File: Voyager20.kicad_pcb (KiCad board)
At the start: 2 copper layers, 73 x 95.2 mm, 92 parts, among them Q1 Q_NPN_BEC, SW1 SW_Push, U1 ATmega32U2-AU, U2 PRTR5V0U2X, Y1 16MHz

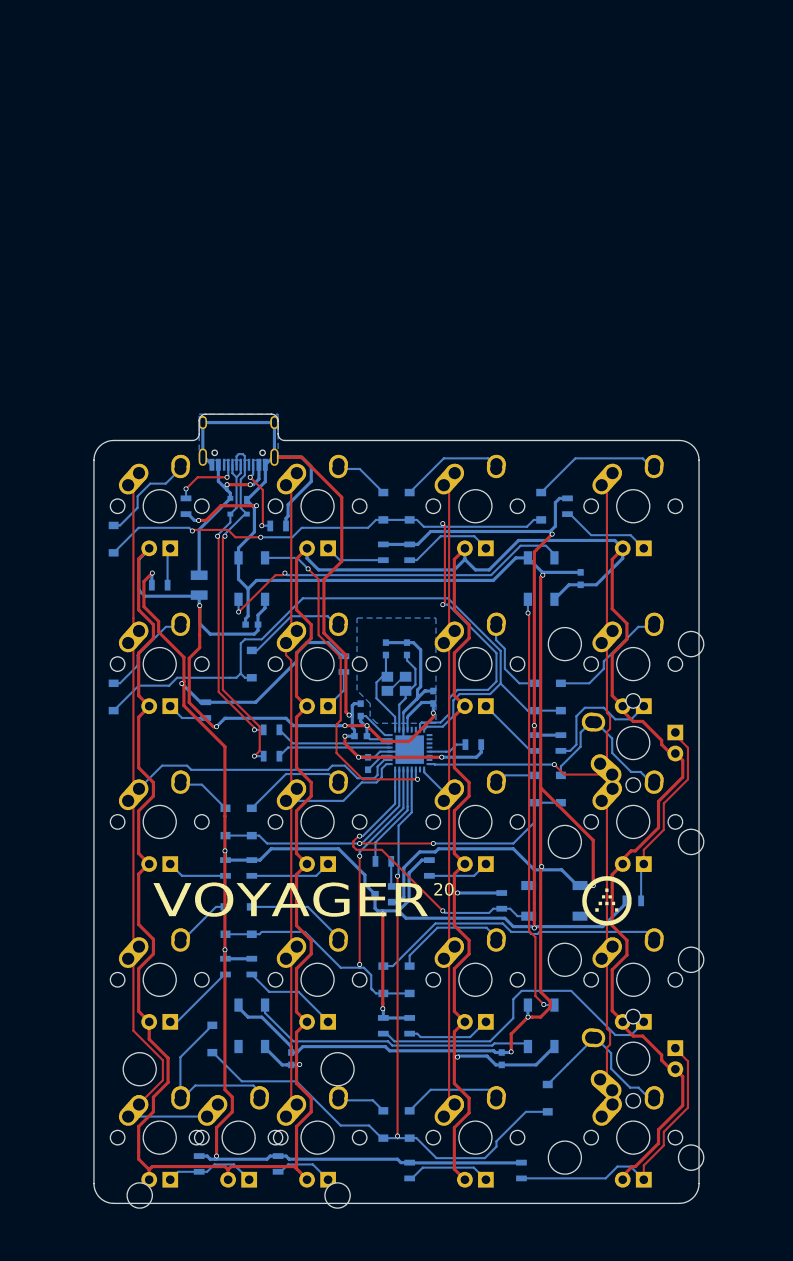
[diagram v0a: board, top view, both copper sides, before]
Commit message: Make 24 key variant
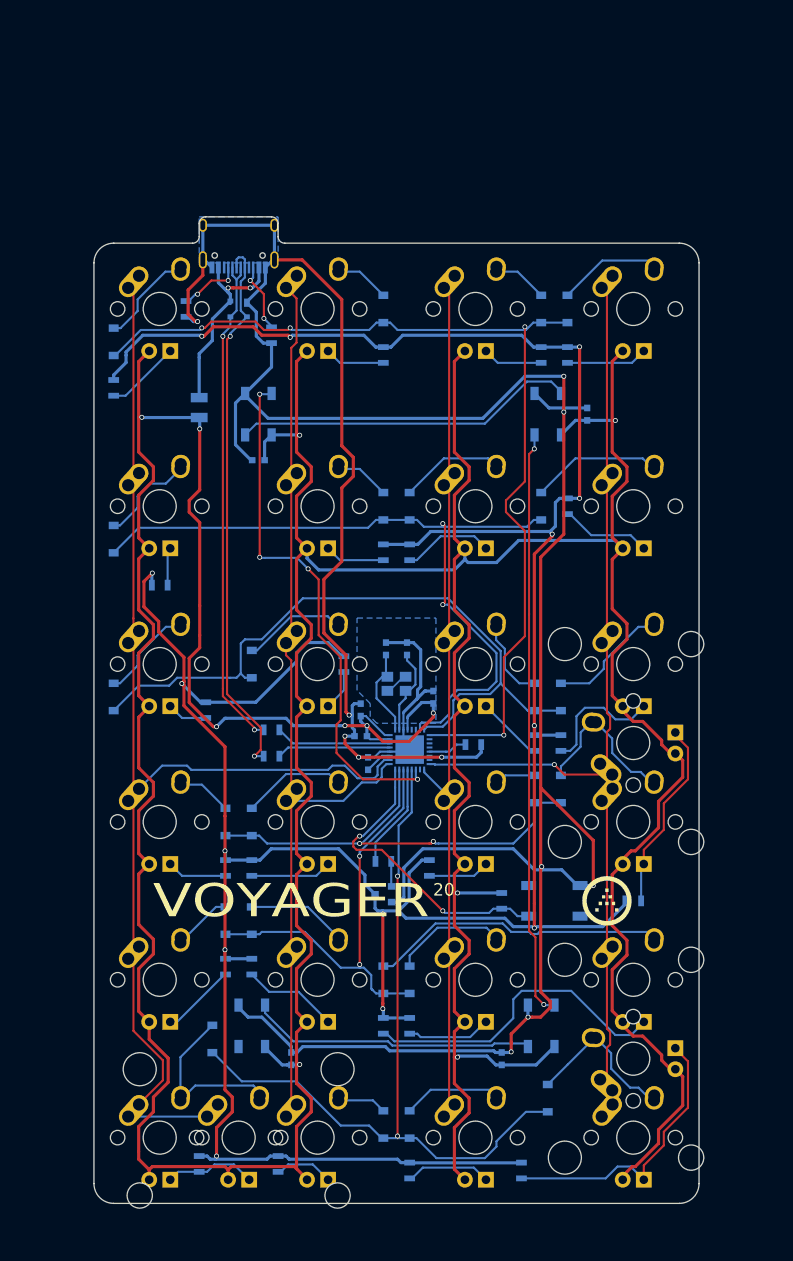
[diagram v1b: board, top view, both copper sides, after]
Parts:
- added D25: SOD-123, Diodes_SMD:D_SOD-123, B.Cu at (42.1, 19.8)
- added D26: SOD-123, Diodes_SMD:D_SOD-123, B.Cu at (74.6, 15.9)
- added D27: SOD-123, Diodes_SMD:D_SOD-123, B.Cu at (93.7, 15.9)
- added D28: SOD-123, Diodes_SMD:D_SOD-123, B.Cu at (96.8, 15.9)
- added MX21: MX-1U, MX_Alps_Hybrid:MX-1U, F.Cu at (47.6, 15.9)
- added MX22: MX-1U, MX_Alps_Hybrid:MX-1U, F.Cu at (66.7, 15.9)
- added MX23: MX-1U, MX_Alps_Hybrid:MX-1U, F.Cu at (85.7, 15.9)
- added MX24: MX-1U, MX_Alps_Hybrid:MX-1U, F.Cu at (104.8, 15.9)
- added R28: 1k, Resistors_SMD:R_0805, B.Cu at (42.1, 25.4)
- added R29: 1k, Resistors_SMD:R_0805, B.Cu at (74.6, 21.4)
- added R30: 1k, Resistors_SMD:R_0805, B.Cu at (93.7, 21.4)
- added R31: 1k, Resistors_SMD:R_0805, B.Cu at (96.8, 21.4)
- moved R6 23.8 mm to (50.8, 15.9)
- moved U2 23.8 mm to (57.1, 15.9)
- moved USB1 23.8 mm to (57.1, 3.17)
- moved R4 23.0 mm to (61.1, 19.1), turned to 270 degrees
- moved F1 21.4 mm to (52.4, 27.8)
- moved CR2 19.9 mm to (99.2, 28.6)
- moved D18 19.9 mm to (94.5, 28.6)
- moved D9 19.9 mm to (59.5, 28.6)
- moved CR1 19.9 mm to (59.5, 34.1)
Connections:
- U1 pad 9: Net-(U1-Pad9) -> ROWFN
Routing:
- net ROWFN: track 0.00 -> 119.8 mm, vias 0 -> 4
- net +5V: track 547.6 -> 658.1 mm, vias 8 -> 11
- net LEDGND: track 308.1 -> 390.4 mm, vias 10 -> 14
- net GND: track 345.4 -> 396.1 mm
- net COL1: track 93.3 -> 118.1 mm
- net COL0: track 123.3 -> 147.7 mm
- net COL2: track 83.1 -> 107.4 mm
- net COL3: track 100.1 -> 124.4 mm
- net Net-(R3-Pad1): track 43.5 -> 66.7 mm
- net Net-(R2-Pad2): track 37.8 -> 61.0 mm
- net RGBLED: track 42.2 -> 64.0 mm, vias 2 -> 4
- net Net-(D18-Pad2): track 51.0 -> 71.1 mm
- net Net-(D28-Pad2): track 0.00 -> 13.3 mm
- net Net-(D25-Pad2): track 0.00 -> 11.7 mm
- net Net-(MX24-Pad4): track 0.00 -> 9.80 mm
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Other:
- board size 73 x 95.2 mm -> 73 x 119.1 mm

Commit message: Route 3700 variant
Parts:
- removed CR1, CR2, CR3, CR4: 0.1u, Capacitors_SMD:C_0603
- removed D18, D23, D24, D9: WS2812B, LEDs:LED_WS2812B-PLCC4
- removed R4, R6: 5.1k, Resistors_SMD:R_0805
- removed USB1: HRO-TYPE-C-31-M-12, Type-C:HRO-TYPE-C-31-M-12-Assembly
- added J1: Conn_01x04, Pin_Headers:Pin_Header_Straight_1x04_Pitch2.54mm, B.Cu at (53.2, -13.5)
- added JP1: JP-INDICATOR, random-keyboard-parts:Jumper-UserFriendly-Small, B.Cu at (54.0, 49.2)
- added JP2: JP-BLIGHT, random-keyboard-parts:Jumper-UserFriendly-Small, B.Cu at (57.1, 49.2)
- added REF**: outline, locallib:outline, F.Cu at (30.4, -19.3)
- added REF**: MountingHole_3.2mm_M3, Mounting_Holes:MountingHole_3.2mm_M3, F.Cu at (71.4, -15.1)
- added REF**: MountingHole_3.2mm_M3, Mounting_Holes:MountingHole_3.2mm_M3, F.Cu at (81.0, -15.1)
- U1: footprint Housings_DFN_QFN:QFN-32-1EP_5x5mm_Pitch0.5mm -> Housings_QFP:TQFP-32_7x7mm_Pitch0.8mm
- moved Q1 101.4 mm to (45.5, -10.6)
- moved R27 101.4 mm to (45.5, -14.6)
- moved SW1 84.2 mm to (43.7, 20.7), turned to 90 degrees
- moved R1 74.7 mm to (43.7, 27.8), turned to 0 degrees
- moved G*** 72.1 mm to (111.1, 15.9)
- moved R3 63.0 mm to (55.6, 7.14), turned to 270 degrees
- moved C3 62.3 mm to (54.8, 11.1), turned to 0 degrees
- moved R2 59.6 mm to (58.7, 7.14), turned to 90 degrees
- moved C5 55.5 mm to (62.7, 12.7), turned to 0 degrees
- moved C6 54.7 mm to (62.7, 10.3), turned to 0 degrees
- moved U1 54.1 mm to (56.9, 19.1), turned to 180 degrees
- moved R5 49.4 mm to (56.4, 28.6), turned to 90 degrees
- moved Y1 45.7 mm to (66.8, 16.4), turned to 270 degrees
- moved C4 43.6 mm to (66.7, 21.4), turned to 0 degrees
- moved C1 41.9 mm to (71.0, 15.2), turned to 0 degrees
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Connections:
- net Net-(MX1-Pad4) renamed NLOCKLED
- R7 pad 2: LEDGND -> Net-(JP1-Pad1)
- U1 pad 10: Net-(U1-Pad10) -> NLCKLED
- U1 pad 19: RGBLED -> Net-(U1-Pad19)
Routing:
- net GND: track 396.1 -> 131.7 mm, vias 11 -> 6
- net ROW3: track 52.5 -> 126.6 mm
- net Net-(D18-Pad2): track 71.1 -> 0.00 mm, vias 2 -> 0
- net RGBLED: track 64.0 -> 0.00 mm, vias 4 -> 0
- net ROW4: track 93.6 -> 150.7 mm, vias 2 -> 5
- net ROW2: track 55.6 -> 111.1 mm
- net Net-(J1-Pad2): track 66.7 -> 20.7 mm, vias 2 -> 0
- net COL3: track 124.4 -> 166.2 mm, vias 1 -> 3
- net COL2: track 107.4 -> 149.0 mm, vias 0 -> 3
- net Net-(D18-Pad4): track 41.5 -> 0.00 mm
- net Net-(J1-Pad3): track 61.0 -> 20.6 mm, vias 2 -> 0
- net COL1: track 118.1 -> 158.1 mm, vias 0 -> 1
- net ROWFN: track 119.8 -> 82.8 mm, vias 4 -> 3
- net NLCKLED: track 0.00 -> 34.8 mm, vias 0 -> 2
- net Net-(D23-Pad2): track 34.6 -> 0.00 mm
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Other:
- board size 73 x 119.1 mm -> 91.5 x 148 mm
- board text added: "1 2 3 4"
- board text added: "3700"
- board text added: "4 3 2 1"
- board text added: "BACKL"
- board text added: "Connection Options a) Hardwire USB cable to USB pads. Optionally zip-tie the cable to the pcb using the hole provided for strength. b) Mount a Mini-XLR connector on the PS2 passthrough hole. Wire to the USB pads, following the numbered order."
- board text added: "GND D+ D- VCC"
- board text added: "IND"
- board text added: "VCC D- D+ GND"
- board text removed: "20"
- board text removed: "Voyager20 PCB Rev 1.0 20190126 kb.ai03.me"
